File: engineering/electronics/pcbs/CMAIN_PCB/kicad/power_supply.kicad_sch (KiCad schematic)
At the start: 108 parts, among them J25 B08B-JWPF-SK-R, J26 B08B-JWPF-SK-R, J28 B08B-JWPF-SK-R, J34 B08B-JWPF-SK-R, J42 B08B-JWPF-SK-R, J44 B08B-JWPF-SK-R, Q4 PSMN4R3-30BL,118, Q5 PSMN4R3-30BL,118, Q6 ${ALTIUM_VALUE}, Q7 ${ALTIUM_VALUE}, Q8 PSMN4R3-30BL,118, Q9 ${ALTIUM_VALUE}, U17 SY8205FCC, U18 SY8205FCC, U29 LTC4370IMS#PBF, U30 LTC4370IMS#PBF, U31 LTC4370IMS#PBF, U4 SY8205FCC

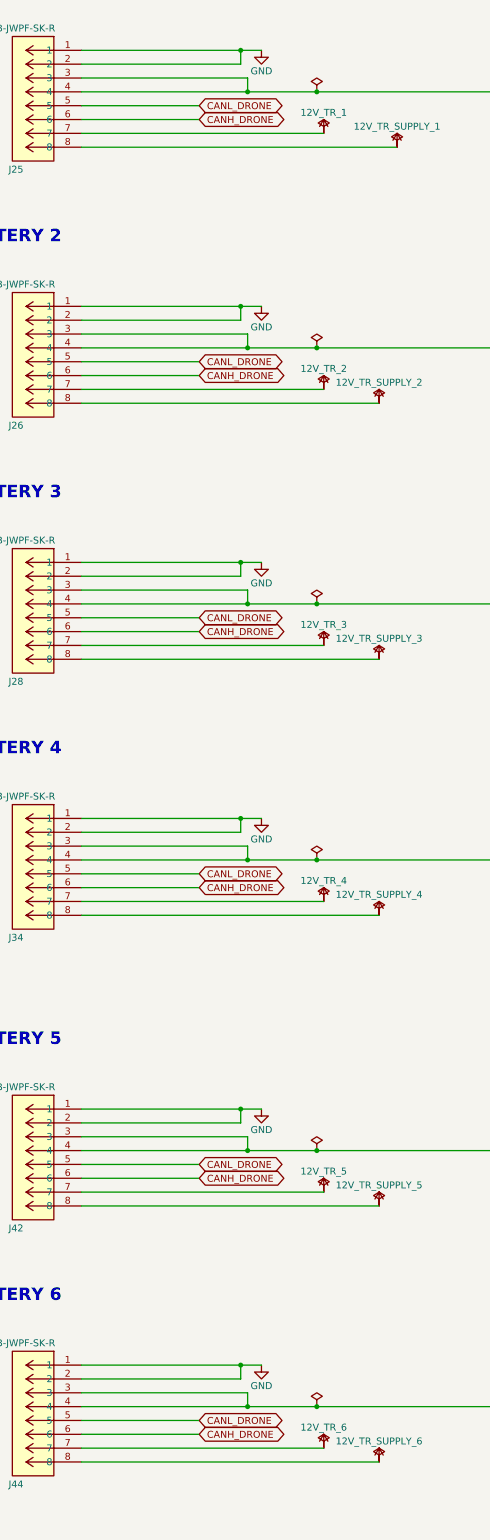
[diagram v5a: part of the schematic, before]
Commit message: Update CMAIN PCB routing from latest archive
Import Julius's latest CMAIN KiCad update, excluding local .history and backup archives. Remap undefined Rescue footprint graphics to F.Fab so KiCad CLI can load the board, and add KiCad ERC/DRC reports.
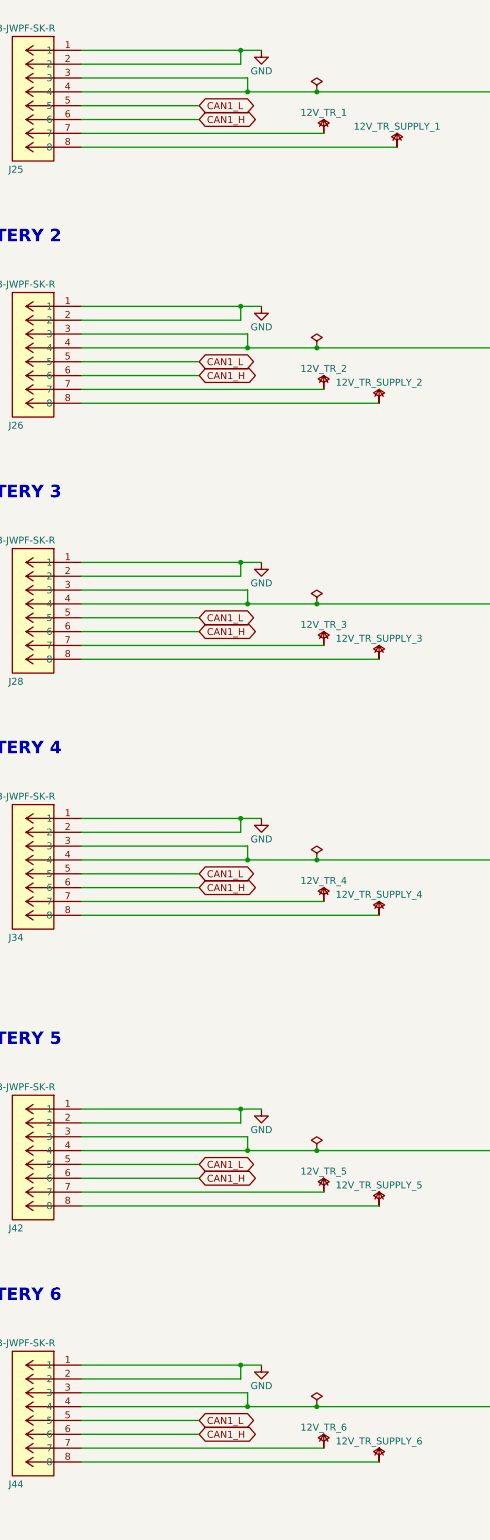
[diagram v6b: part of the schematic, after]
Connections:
- net CANH_DRONE renamed CAN1_H
- net CANL_DRONE renamed CAN1_L

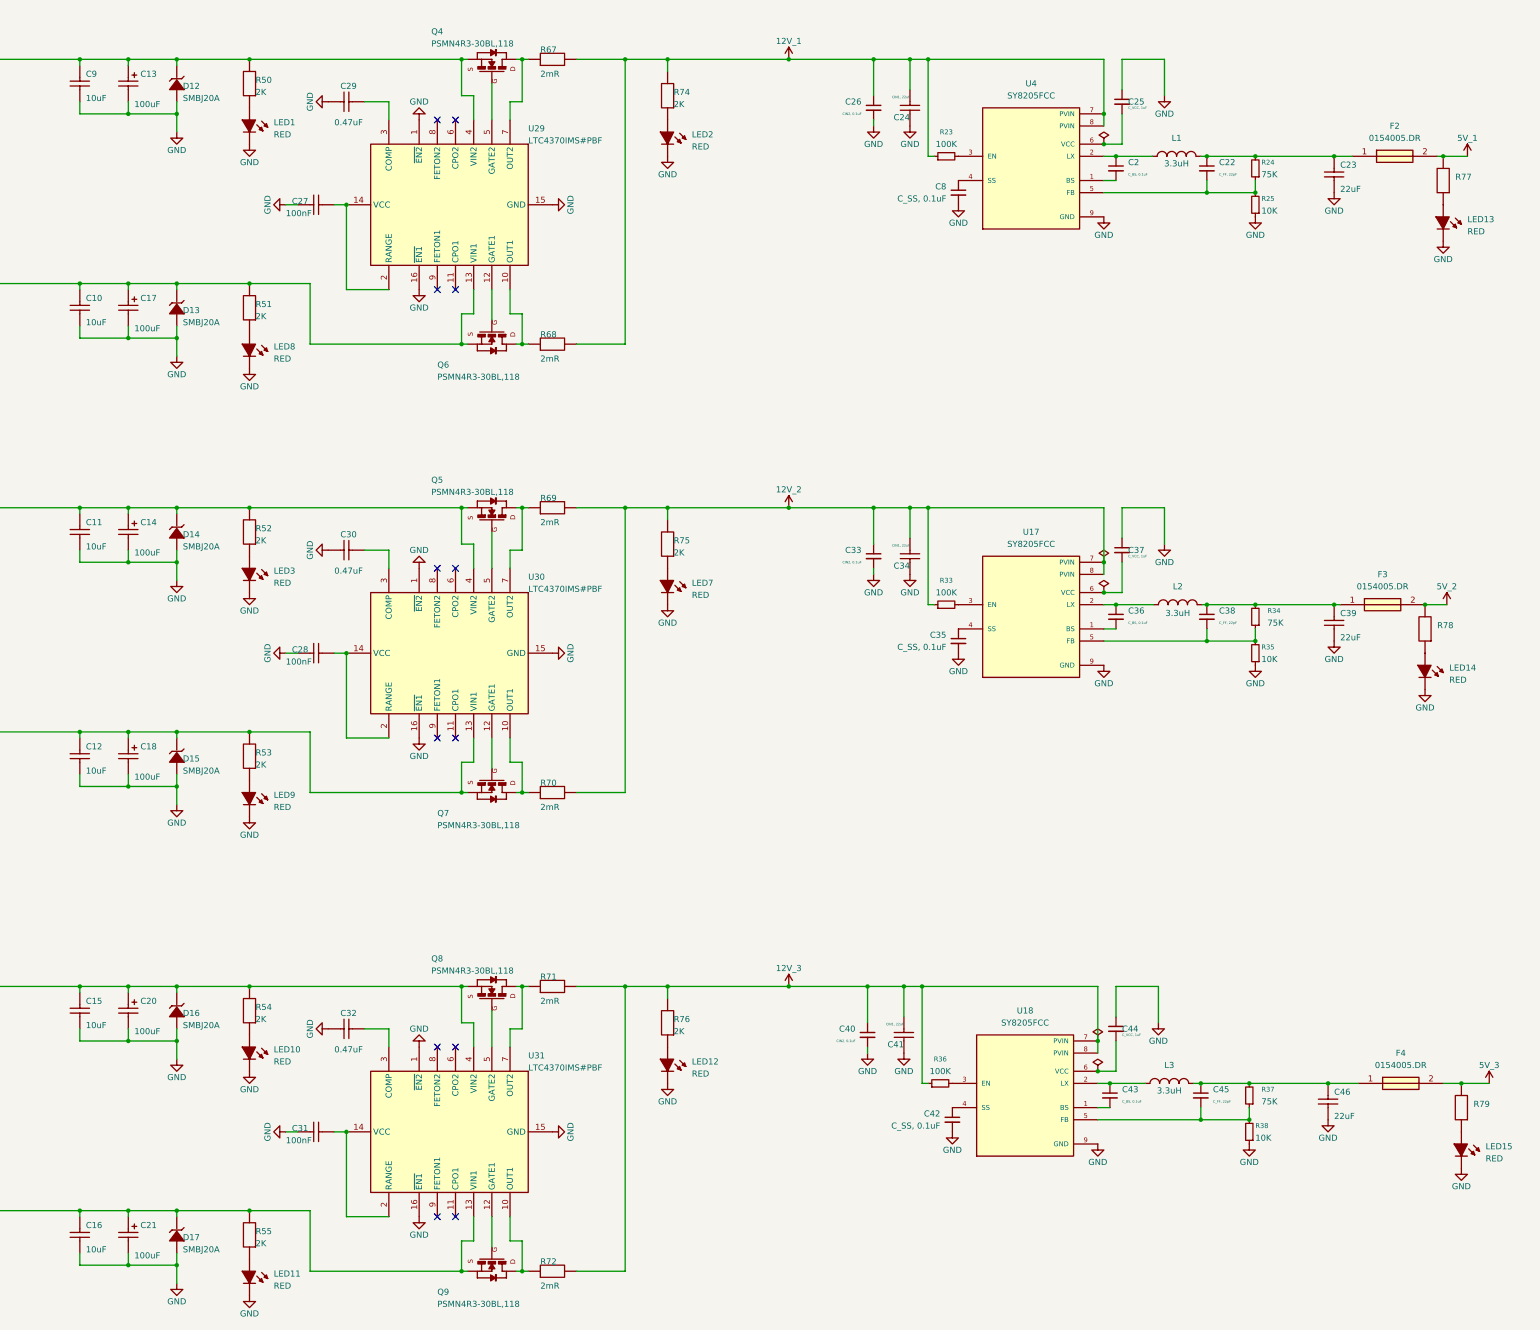
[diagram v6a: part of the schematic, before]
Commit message: Clean up CMAIN part value fields
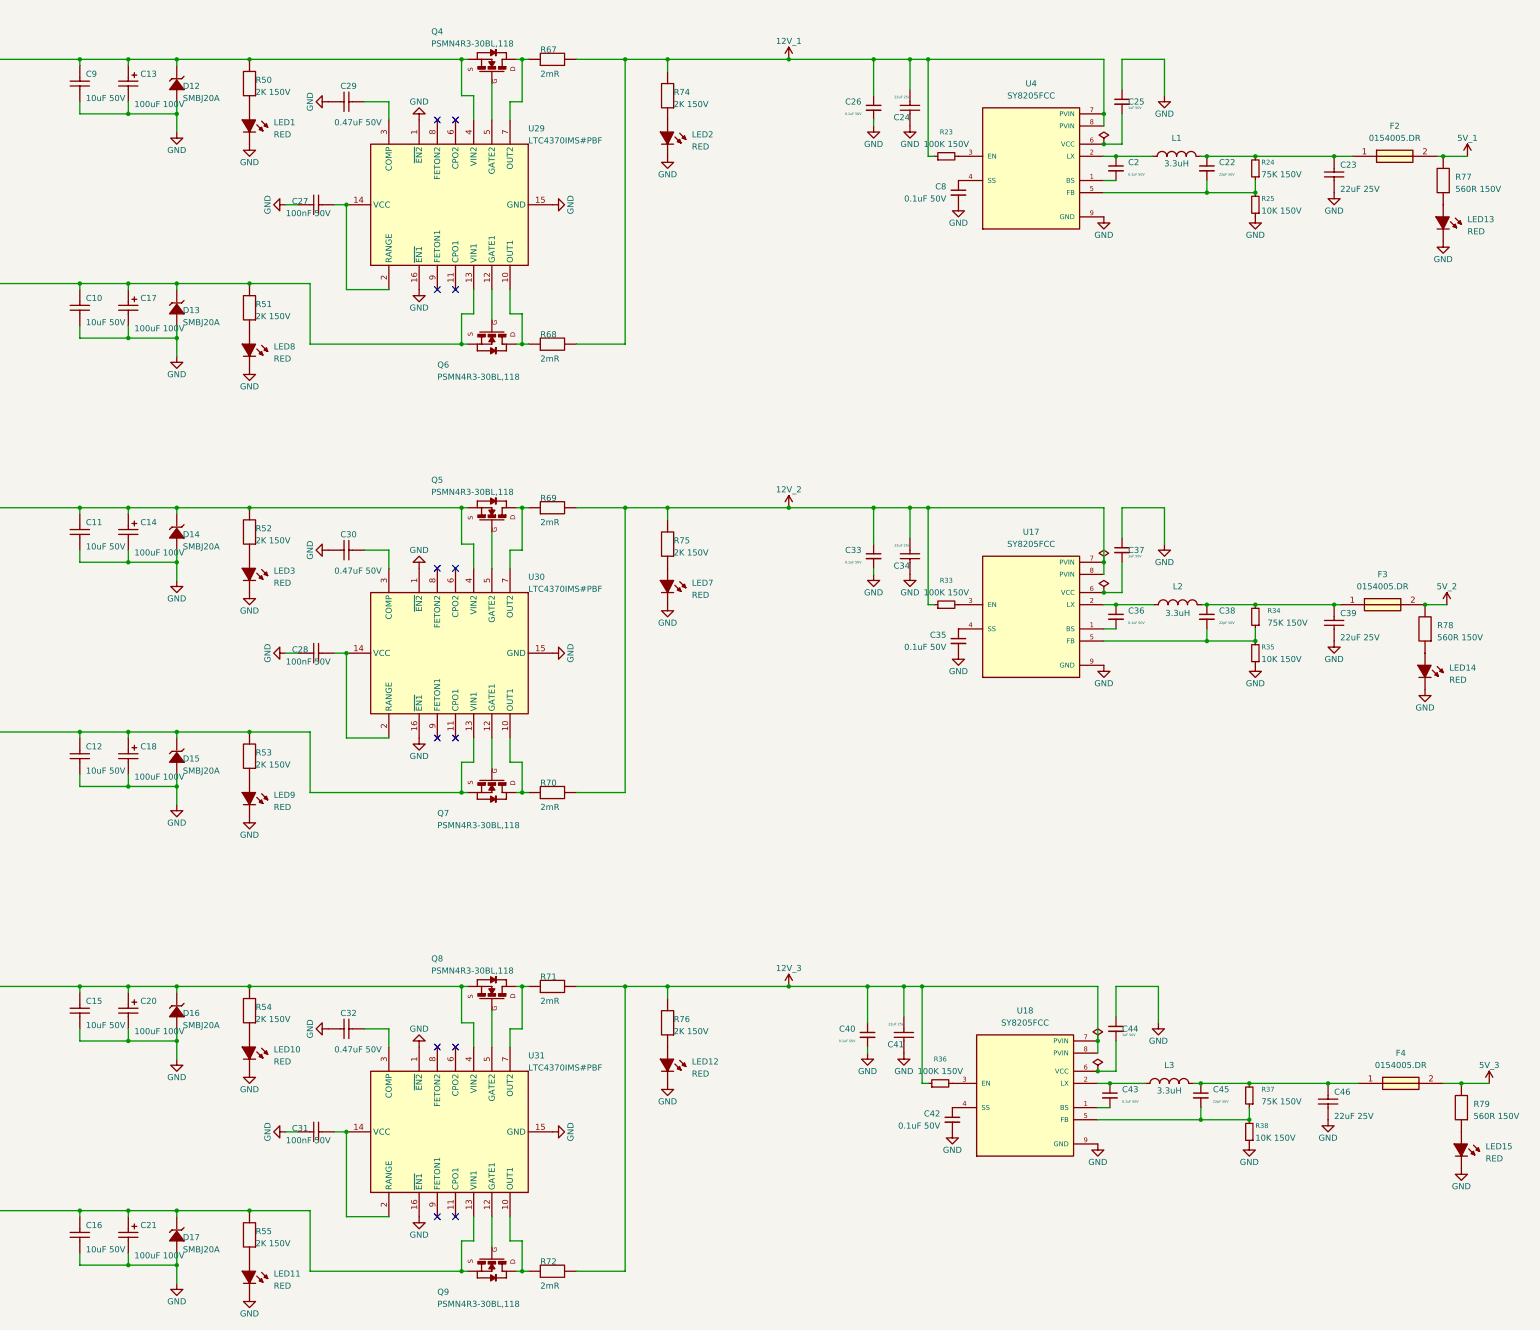
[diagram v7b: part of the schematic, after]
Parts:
- C10, C11, C12, C15, C16, C9: value ${ALTIUM_VALUE} -> 10uF 50V
- C13, C14, C17, C18, C20, C21: value ${ALTIUM_VALUE} -> 100uF 100V
- C2, C36, C43: value C_BS, 0.1uF -> 0.1uF 50V; footprint CMAIN_PCB:fp_71505040a9 -> Capacitor_SMD:C_0805_2012Metric_Pad1.18x1.45mm_HandSolder
- C22: value C_FF, 22pF -> 22pF 50V; footprint CMAIN_PCB:fp_6a12138141 -> Capacitor_SMD:C_0603_1608Metric_Pad1.08x0.95mm_HandSolder
- C23, C39, C46: value 22uF -> 22uF 25V
- C24, C34, C41: value CIN1, 22uF -> 22uF 25V
- C25, C37, C44: value C_VCC, 1uF -> 1uF 50V; footprint CMAIN_PCB:fp_71505040a9 -> Capacitor_SMD:C_0805_2012Metric_Pad1.18x1.45mm_HandSolder
- C26, C33, C40: value CIN2, 0.1uF -> 0.1uF 50V; footprint CMAIN_PCB:fp_71505040a9 -> Capacitor_SMD:C_0805_2012Metric_Pad1.18x1.45mm_HandSolder
- C27, C28, C31: value ${ALTIUM_VALUE} -> 100nF 50V; footprint CMAIN_PCB:fp_71505040a9 -> Capacitor_SMD:C_0805_2012Metric_Pad1.18x1.45mm_HandSolder
- C29, C30, C32: value ${ALTIUM_VALUE} -> 0.47uF 50V; footprint CMAIN_PCB:fp_71505040a9 -> Capacitor_SMD:C_0805_2012Metric_Pad1.18x1.45mm_HandSolder
- C35, C42, C8: value C_SS, 0.1uF -> 0.1uF 50V; footprint CMAIN_PCB:fp_71505040a9 -> Capacitor_SMD:C_0805_2012Metric_Pad1.18x1.45mm_HandSolder
- C38, C45: value C_FF, 22pF -> 22pF 50V
- D12, D13, D14, D15, D16, D17: value ${ALTIUM_VALUE} -> SMBJ20A
- LED1, LED10, LED11, LED12, LED13, LED14, LED15, LED2, LED3, LED7, LED8, LED9: value ${ALTIUM_VALUE} -> RED
- Q6, Q7, Q9: value ${ALTIUM_VALUE} -> PSMN4R3-30BL,118
- R23, R33, R36: value 100K -> 100K 150V; footprint CMAIN_PCB:fp_9fb50b8536 -> Resistor_SMD:R_0805_2012Metric_Pad1.20x1.40mm_HandSolder
- R24, R34, R37: value 75K -> 75K 150V; footprint CMAIN_PCB:fp_9fb50b8536 -> Resistor_SMD:R_0805_2012Metric_Pad1.20x1.40mm_HandSolder
- R25, R35, R38: value 10K -> 10K 150V; footprint CMAIN_PCB:fp_9fb50b8536 -> Resistor_SMD:R_0805_2012Metric_Pad1.20x1.40mm_HandSolder
- R50, R51, R52, R53, R54, R55, R74, R75, R76: value ${ALTIUM_VALUE} -> 2K 150V; footprint CMAIN_PCB:fp_9fb50b8536 -> Resistor_SMD:R_0805_2012Metric_Pad1.20x1.40mm_HandSolder
- R67, R68, R69, R70, R71, R72: value ${ALTIUM_VALUE} -> 2mR; footprint CMAIN_PCB:R_2512_6332Metric -> Resistor_SMD:R_2512_6332Metric
- R77, R78, R79: value (none) -> 560R 150V; footprint CMAIN_PCB:fp_9fb50b8536 -> Resistor_SMD:R_0805_2012Metric_Pad1.20x1.40mm_HandSolder
